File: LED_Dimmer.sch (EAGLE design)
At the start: 12 parts

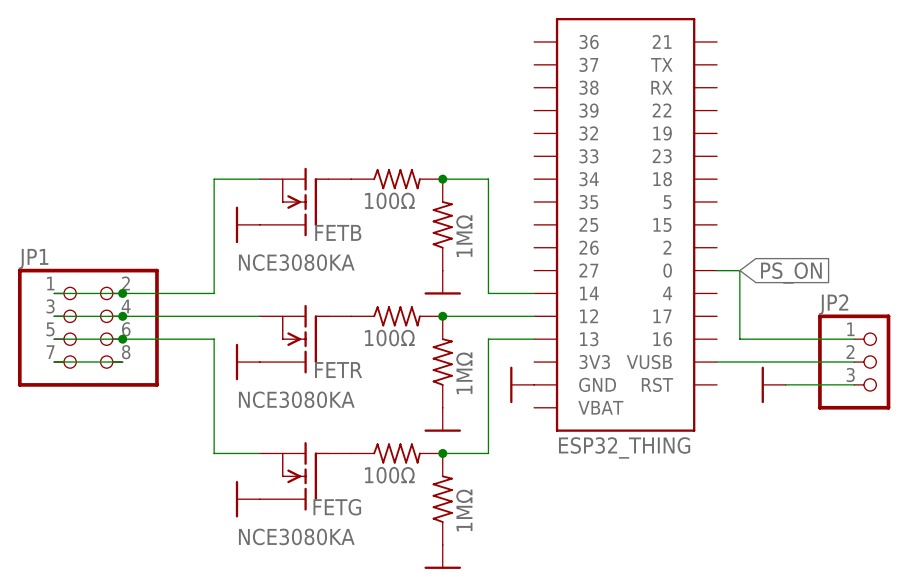
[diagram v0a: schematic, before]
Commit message: Swapped Fet Drain and Source
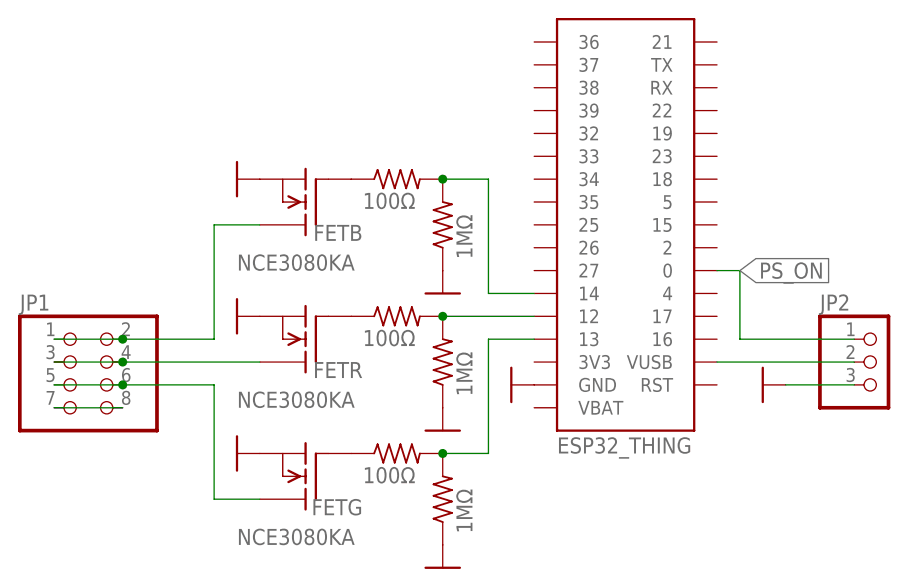
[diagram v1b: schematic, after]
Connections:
- removed net N$5: FETR.S, JP1.3, JP1.4
- new net N$7: FETR.D, JP1.3, JP1.4
- net GND: now also FETB.S, FETG.S, FETR.S; no longer FETB.D, FETG.D, FETR.D
- net N$4: now also FETB.D; no longer FETB.S
- net N$6: now also FETG.D; no longer FETG.S
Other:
- moved on the sheet: JP1
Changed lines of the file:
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@@
 <part name="FETB" library="Personal" deviceset="NCE3080KA" device=""/>
 <part name="GND2" library="supply1" library_urn="urn:adsk.eagle:library:371" deviceset="GND" device=""/>
-<part name="GND3" library="supply1" library_urn="urn:adsk.eagle:library:371" deviceset="GND" device=""/>
-<part name="GND4" library="supply1" library_urn="urn:adsk.eagle:library:371" deviceset="GND" device=""/>
-<part name="GND5" library="supply1" library_urn="urn:adsk.eagle:library:371" deviceset="GND" device=""/>
 <part name="JP2" library="pinhead" library_urn="urn:adsk.eagle:library:325" deviceset="PINHD-1X3" device="/90" package3d_urn="urn:adsk.eagle:package:22459/2"/>
 <part name="GND1" library="supply1" library_urn="urn:adsk.eagle:library:371" deviceset="GND" device=""/>
@@
 <part name="GND8" library="supply1" library_urn="urn:adsk.eagle:library:371" deviceset="GND" device=""/>
 <part name="JP1" library="pinhead" library_urn="urn:adsk.eagle:library:325" deviceset="PINHD-2X4" device="" package3d_urn="urn:adsk.eagle:package:22461/2"/>
+<part name="GND4" library="supply1" library_urn="urn:adsk.eagle:library:371" deviceset="GND" device=""/>
+<part name="GND9" library="supply1" library_urn="urn:adsk.eagle:library:371" deviceset="GND" device=""/>
+<part name="GND3" library="supply1" library_urn="urn:adsk.eagle:library:371" deviceset="GND" device=""/>
 </parts>
 <sheets>
@@
 </instance>
 <instance part="GND2" gate="1" x="-12.7" y="-20.32" smashed="yes" rot="R270"/>
-<instance part="GND3" gate="1" x="-43.18" y="-33.02" smashed="yes" rot="R270"/>
-<instance part="GND4" gate="1" x="-43.18" y="-17.78" smashed="yes" rot="R270"/>
-<instance part="GND5" gate="1" x="-43.18" y="-2.54" smashed="yes" rot="R270"/>
 <instance part="JP2" gate="A" x="27.94" y="-17.78" smashed="yes">
 <attribute name="NAME" x="21.59" y="-12.065" size="1.778" layer="95"/>
@@
 <instance part="GND7" gate="1" x="-20.32" y="-25.4" smashed="yes"/>
 <instance part="GND8" gate="1" x="-20.32" y="-10.16" smashed="yes"/>
-<instance part="JP1" gate="A" x="-60.96" y="-15.24" smashed="yes">
-<attribute name="NAME" x="-67.31" y="-6.985" size="1.778" layer="95"/>
-<attribute name="VALUE" x="-67.31" y="-22.86" size="1.778" layer="96"/>
-</instance>
+<instance part="JP1" gate="A" x="-60.96" y="-20.32" smashed="yes">
+<attribute name="NAME" x="-67.31" y="-12.065" size="1.778" layer="95"/>
+<attribute name="VALUE" x="-67.31" y="-27.94" size="1.778" layer="96"/>
+</instance>
+<instance part="GND4" gate="1" x="-43.18" y="-12.7" smashed="yes" rot="R270"/>
+<instance part="GND9" gate="1" x="-43.18" y="2.54" smashed="yes" rot="R270"/>
+<instance part="GND3" gate="1" x="-43.18" y="-27.94" smashed="yes" rot="R270"/>
 </instances>
 <busses>
 </busses>
 <nets>
-<net name="N$4" class="0">
-<segment>
-<wire x1="-45.72" y1="-10.16" x2="-45.72" y2="2.54" width="0.1524" layer="91"/>
-<pinref part="FETB" gate="G$1" pin="S"/>
-<wire x1="-45.72" y1="2.54" x2="-40.64" y2="2.54" width="0.1524" layer="91"/>
-<wire x1="-45.72" y1="-10.16" x2="-55.88" y2="-10.16" width="0.1524" layer="91"/>
-<pinref part="JP1" gate="A" pin="2"/>
-<pinref part="JP1" gate="A" pin="1"/>
-<wire x1="-55.88" y1="-10.16" x2="-63.5" y2="-10.16" width="0.1524" layer="91"/>
-<junction x="-55.88" y="-10.16"/>
-</segment>
-</net>
-<net name="N$5" class="0">
-<segment>
-<pinref part="FETR" gate="G$1" pin="S"/>
-<wire x1="-55.88" y1="-12.7" x2="-40.64" y2="-12.7" width="0.1524" layer="91"/>
-<pinref part="JP1" gate="A" pin="4"/>
-<pinref part="JP1" gate="A" pin="3"/>
-<wire x1="-63.5" y1="-12.7" x2="-55.88" y2="-12.7" width="0.1524" layer="91"/>
-<junction x="-55.88" y="-12.7"/>
-</segment>
-</net>
 <net name="N$6" class="0">
 <segment>
-<pinref part="FETG" gate="G$1" pin="S"/>
-<wire x1="-45.72" y1="-15.24" x2="-45.72" y2="-27.94" width="0.1524" layer="91"/>
-<wire x1="-45.72" y1="-27.94" x2="-40.64" y2="-27.94" width="0.1524" layer="91"/>
-<wire x1="-45.72" y1="-15.24" x2="-55.88" y2="-15.24" width="0.1524" layer="91"/>
 <pinref part="JP1" gate="A" pin="6"/>
 <pinref part="JP1" gate="A" pin="5"/>
-<wire x1="-55.88" y1="-15.24" x2="-63.5" y2="-15.24" width="0.1524" layer="91"/>
-<junction x="-55.88" y="-15.24"/>
+<wire x1="-55.88" y1="-20.32" x2="-63.5" y2="-20.32" width="0.1524" layer="91"/>
+<pinref part="FETG" gate="G$1" pin="D"/>
+<wire x1="-40.64" y1="-33.02" x2="-45.72" y2="-33.02" width="0.1524" layer="91"/>
+<wire x1="-45.72" y1="-33.02" x2="-45.72" y2="-20.32" width="0.1524" layer="91"/>
+<wire x1="-45.72" y1="-20.32" x2="-55.88" y2="-20.32" width="0.1524" layer="91"/>
+<junction x="-55.88" y="-20.32"/>
 </segment>
 </net>
@@
 </segment>
 <segment>
-<pinref part="GND3" gate="1" pin="GND"/>
-<pinref part="FETG" gate="G$1" pin="D"/>
-</segment>
-<segment>
-<pinref part="GND4" gate="1" pin="GND"/>
-<pinref part="FETR" gate="G$1" pin="D"/>
-</segment>
-<segment>
-<pinref part="GND5" gate="1" pin="GND"/>
-<pinref part="FETB" gate="G$1" pin="D"/>
-</segment>
-<segment>
 <pinref part="GND1" gate="1" pin="GND"/>
 <pinref part="JP2" gate="A" pin="3"/>
@@
 <pinref part="R4" gate="G$1" pin="1"/>
 <pinref part="GND6" gate="1" pin="GND"/>
+</segment>
+<segment>
+<pinref part="GND4" gate="1" pin="GND"/>
+<pinref part="FETR" gate="G$1" pin="S"/>
+</segment>
+<segment>
+<pinref part="FETB" gate="G$1" pin="S"/>
+<pinref part="GND9" gate="1" pin="GND"/>
+</segment>
+<segment>
+<pinref part="FETG" gate="G$1" pin="S"/>
+<pinref part="GND3" gate="1" pin="GND"/>
 </segment>
 </net>
@@
 <pinref part="JP1" gate="A" pin="7"/>
 <pinref part="JP1" gate="A" pin="8"/>
+<wire x1="-63.5" y1="-22.86" x2="-55.88" y2="-22.86" width="0.1524" layer="91"/>
+</segment>
+</net>
+<net name="N$7" class="0">
+<segment>
+<pinref part="JP1" gate="A" pin="4"/>
+<pinref part="JP1" gate="A" pin="3"/>
 <wire x1="-63.5" y1="-17.78" x2="-55.88" y2="-17.78" width="0.1524" layer="91"/>
-</segment>
-</net>
+<pinref part="FETR" gate="G$1" pin="D"/>
+<wire x1="-40.64" y1="-17.78" x2="-55.88" y2="-17.78" width="0.1524" layer="91"/>
+<junction x="-55.88" y="-17.78"/>
+</segment>
+</net>
+<net name="N$4" class="0">
+<segment>
+<pinref part="FETB" gate="G$1" pin="D"/>
+<wire x1="-40.64" y1="-2.54" x2="-45.72" y2="-2.54" width="0.1524" layer="91"/>
+<wire x1="-45.72" y1="-2.54" x2="-45.72" y2="-15.24" width="0.1524" layer="91"/>
+<pinref part="JP1" gate="A" pin="2"/>
+<pinref part="JP1" gate="A" pin="1"/>
+<wire x1="-55.88" y1="-15.24" x2="-63.5" y2="-15.24" width="0.1524" layer="91"/>
+<wire x1="-45.72" y1="-15.24" x2="-55.88" y2="-15.24" width="0.1524" layer="91"/>
+<junction x="-55.88" y="-15.24"/>
+</segment>
+</net>
